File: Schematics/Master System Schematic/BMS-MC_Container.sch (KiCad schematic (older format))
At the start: 8 parts, among them K1 Cooling Pump Shutoff Relay, K54 Cooling Pump Relay, U3 RinehartPM100DX_MotorControll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

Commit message: Improved BMS schematic spacing
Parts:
- gave numbers to parts that had none: 5
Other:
- moved on the sheet: D31, D32, K1, K53, K54, U3, U6, U7

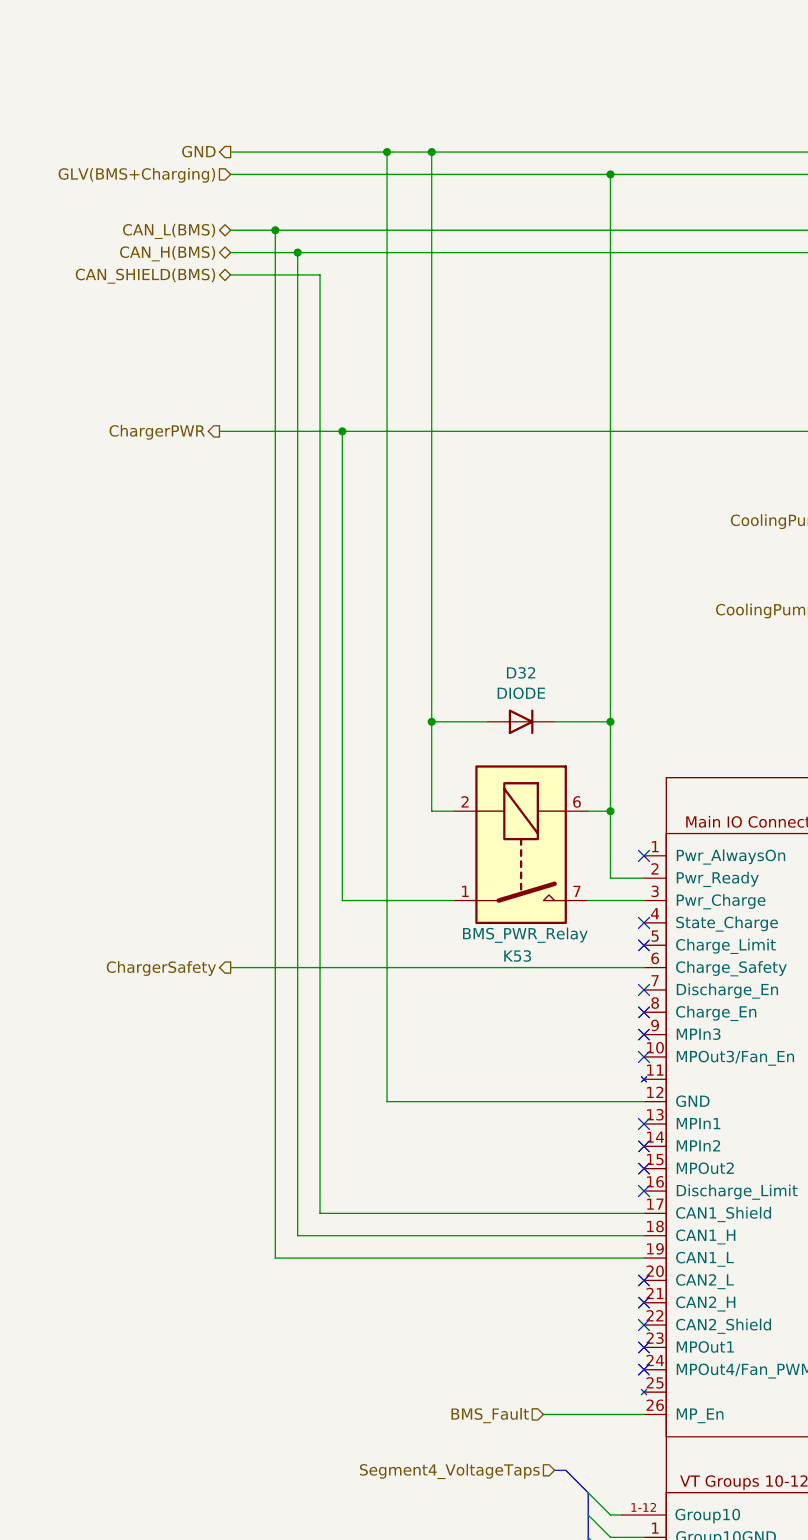
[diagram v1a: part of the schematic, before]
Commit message: Added a BMS Fan
BMS Fan was required for cooling purposes of the enclosure. I added it. Not sure if this was done correctly though. Especially with the portion for pos and neg ends connected to the BMS itself.
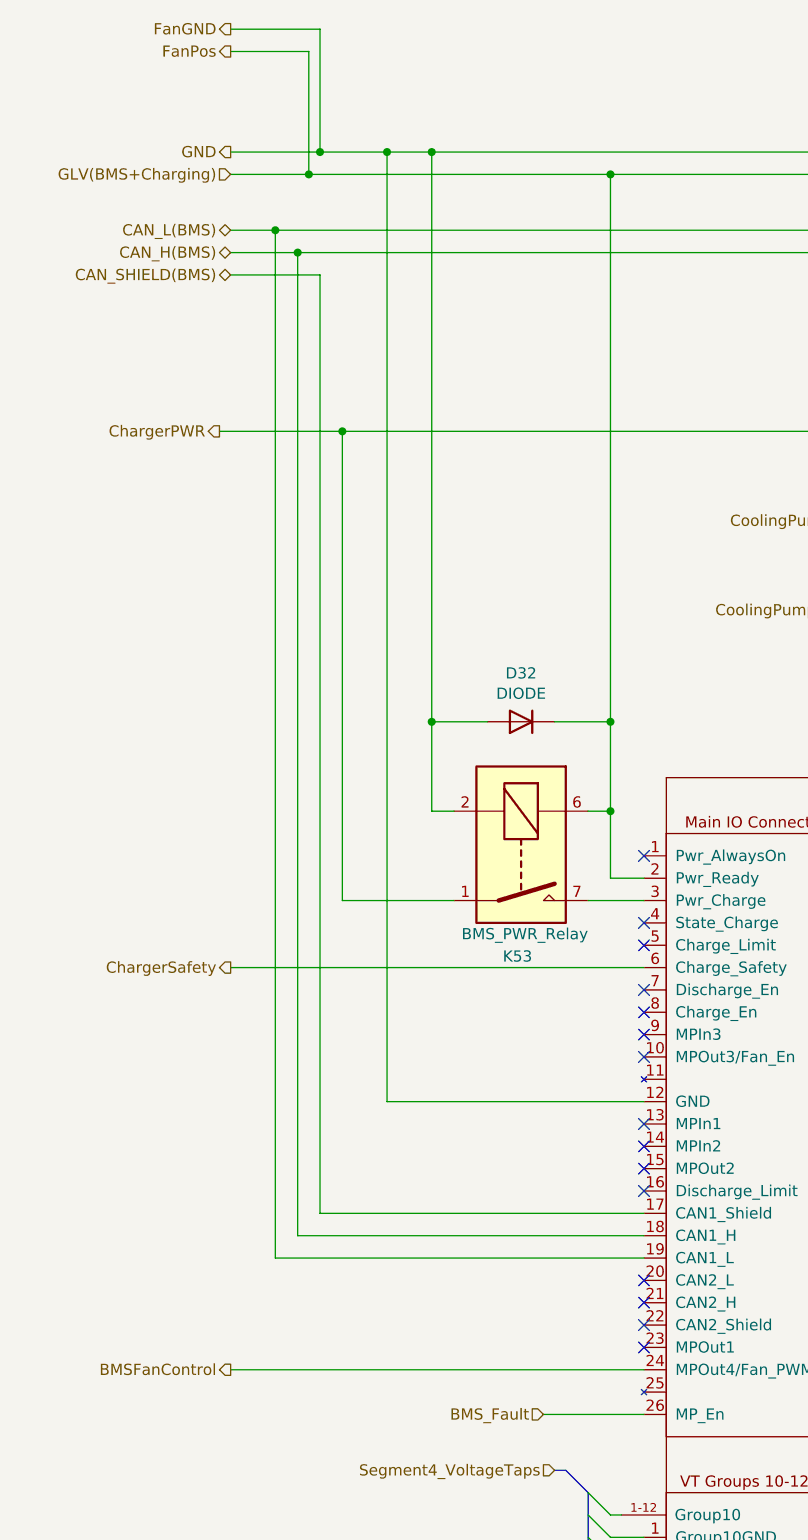
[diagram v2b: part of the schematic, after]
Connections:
- net GLV(BMS+Charging) is gone; now on net FanPos: D32.2 (K), K53.6, U6.2 (RM1-), U7.2 (PowerA)
- net GND is gone; now on net FanGND: D32.1 (A), K1.5, K53.2, K54.6, U3.14 (XDCR_PWR), U3.6 (GND), U6.12 (GND), U7.4 (GND)
- net FanPos: now reaches U6.2 (RM1-)
- net BMSFanControl: now reaches U6.24 (MPOut4/Fan_PWM)
- net at U6.3 (RM2+): now also K53.7, K53.8
- net FanGND: now reaches U3.14 (XDCR_PWR)
- no-connect marks 29 -> 28
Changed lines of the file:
@@
 EESchema Schematic File Version 4
-LIBS:Master System Schematic-cache
 EELAYER 30 0
 EELAYER END
 $Descr B 17000 11000
 encoding utf-8
-Sheet 21 22
+Sheet 22 22
 Title "BMS & MC Container"
 Date "2020-11-03"
@@
 NoConn ~ 3500 6500
 NoConn ~ 3500 6600
-NoConn ~ 3500 6700
 Wire Wire Line
 	10100 5000 10350 5000
@@
 	1650 1600 1850 1600
 Wire Wire Line
-	1650 1250 2350 1250
-Wire Wire Line
 	1650 1700 1950 1700
 Wire Wire Line
@@
 	2350 1250 2550 1250
 Wire Wire Line
-	1650 1350 3350 1350
+	1650 1350 2000 1350
 Wire Wire Line
 	2550 1250 2550 3800
@@
 	3350 1350 10450 1350
 Connection ~ 3350 3800
+Wire Wire Line
+	3500 6700 1650 6700
+Text HLabel 1650 6700 0    50   Output ~ 0
+BMSFanControl
+Wire Wire Line
+	1650 1250 2050 1250
+Text HLabel 1650 800  0    50   Output ~ 0
+FanPos
+Text HLabel 1650 700  0    50   Output ~ 0
+FanGND
+Wire Wire Line
+	1650 800  2000 800
+Wire Wire Line
+	2000 800  2000 1350
+Connection ~ 2000 1350
+Wire Wire Line
+	2000 1350 3350 1350
+Wire Wire Line
+	1650 700  2050 700
+Wire Wire Line
+	2050 700  2050 1250
 Wire Bus Line
 	5650 8200 5650 8500
@@
 Wire Bus Line
 	10350 6250 10350 6950
+Connection ~ 2050 1250
+Wire Wire Line
+	2050 1250 2350 1250
 $EndSCHEMATC
